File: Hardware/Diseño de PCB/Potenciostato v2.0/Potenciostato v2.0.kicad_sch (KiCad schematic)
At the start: 31 parts, among them J1 Conn_Coaxial, J2 Conn_02x15_Odd_Even, J3 Conn_Coaxial, J5 Conn_Coaxial, J7 USB_B_Micro, U6 AMS1117-3.3, U7 AMS1117-5.0

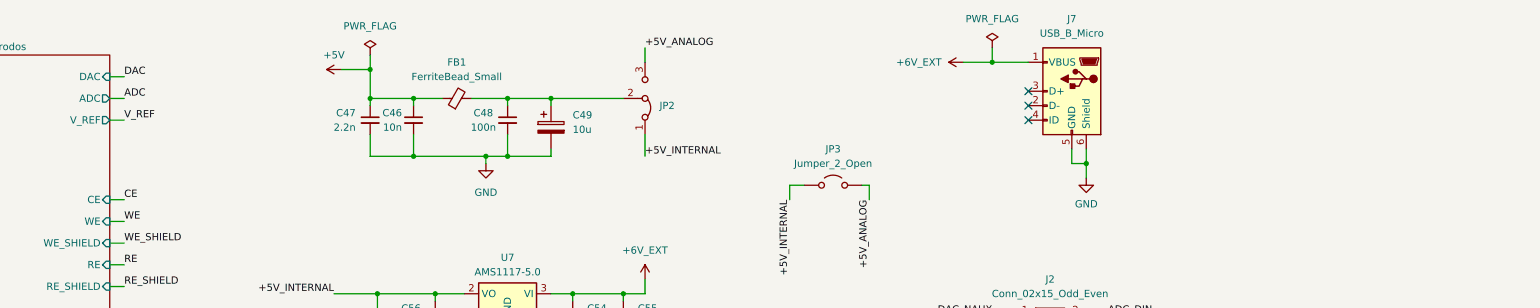
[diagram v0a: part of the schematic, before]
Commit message: Big commit. Hardware was already ready. Board arrived. Hardware testing phase and software development is ongoing, some hardware issues were detected and noted down in the KiCad project for future versions and design corrections. First software libraries under development for ADC, GPIO, Muxes and DAC managment (ADS1255, MAX5217, MAX4737, MAX4617 and GPIO)
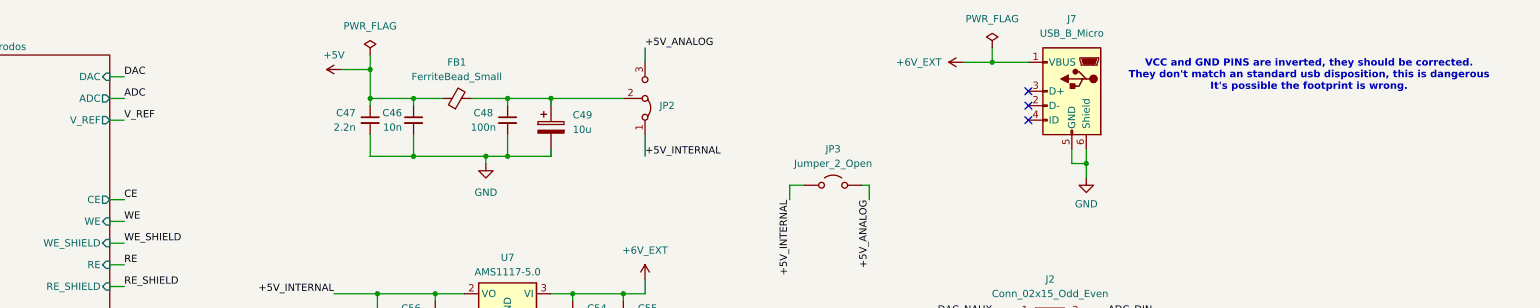
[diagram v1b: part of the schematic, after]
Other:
- note added: "VCC and GND PINS are inverted, they should be corrected. They don't match an standard usb disposition, this is dangerous It's possible the footprint is wrong."
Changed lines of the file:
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@@
 		)
 	)
+	(text "VCC and GND PINS are inverted, they should be corrected.\nThey don't match an standard usb disposition, this is dangerous\nIt's possible the footprint is wrong.\n"
+		(exclude_from_sim no)
+		(at 294.386 28.956 0)
+		(effects
+			(font
+				(size 1.27 1.27)
+				(thickness 0.254)
+				(bold yes)
+				(color 255 0 4 1)
+			)
+		)
+	)
 	(label "DAC_SCL"
 		(at 238.76 73.66 180)
@@
 			)
 		)
-		(pin "CE" input
+		(pin "CE" output
 			(at 83.82 50.8 0)
 			(effects

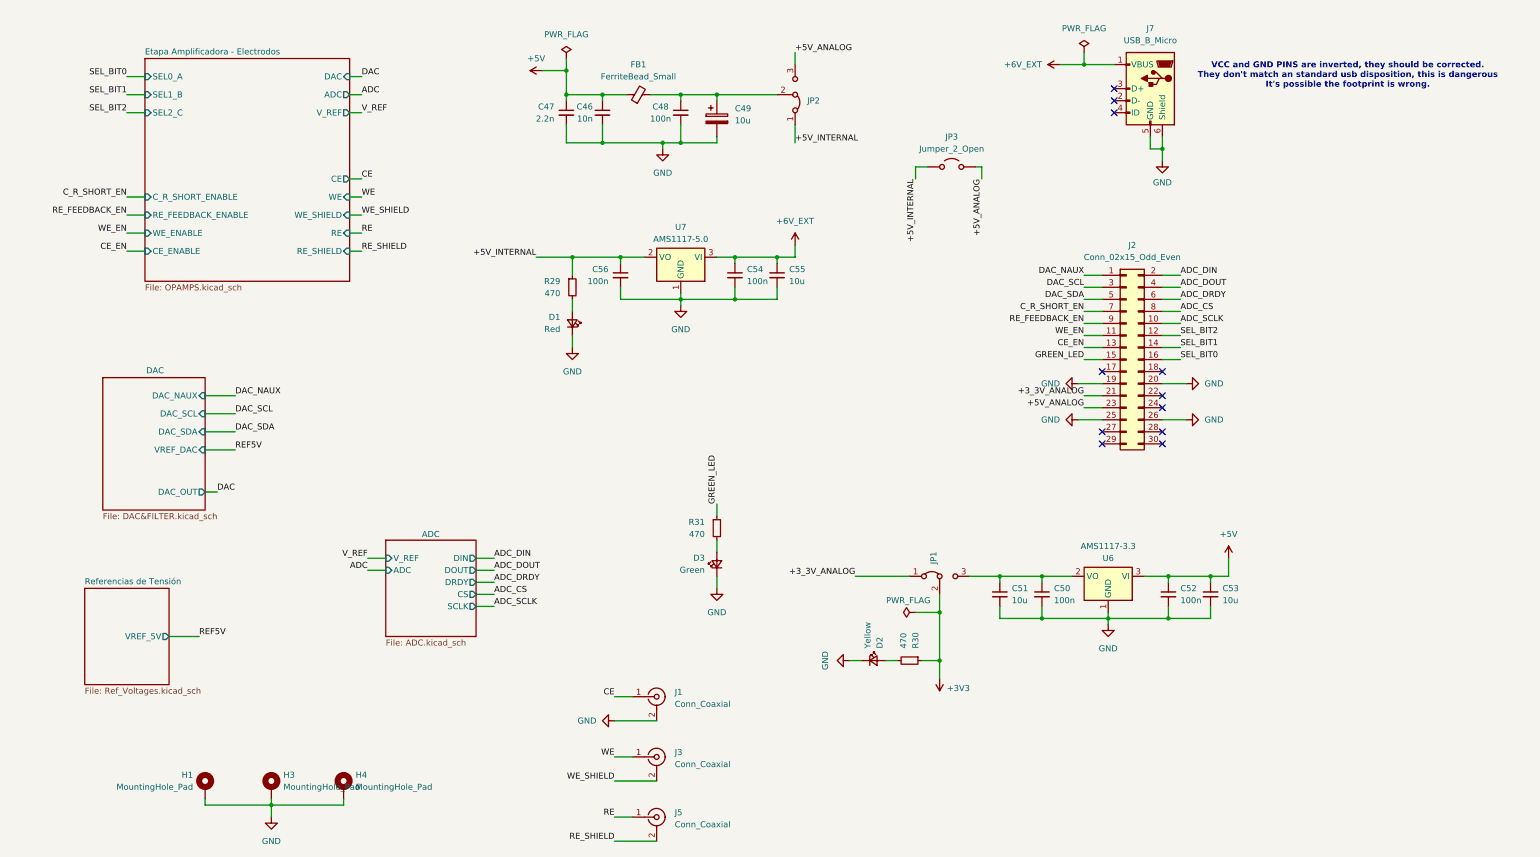
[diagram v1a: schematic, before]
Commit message: Hardware modifications. More notes added to the KiCad project related to hardware issues found during testing. USB Power and ground inverted corrected in design and PCB. MAX4477 replaced by OPA2320 in design and PCB. More notes with recommendations and advised can now be found in the schematics.
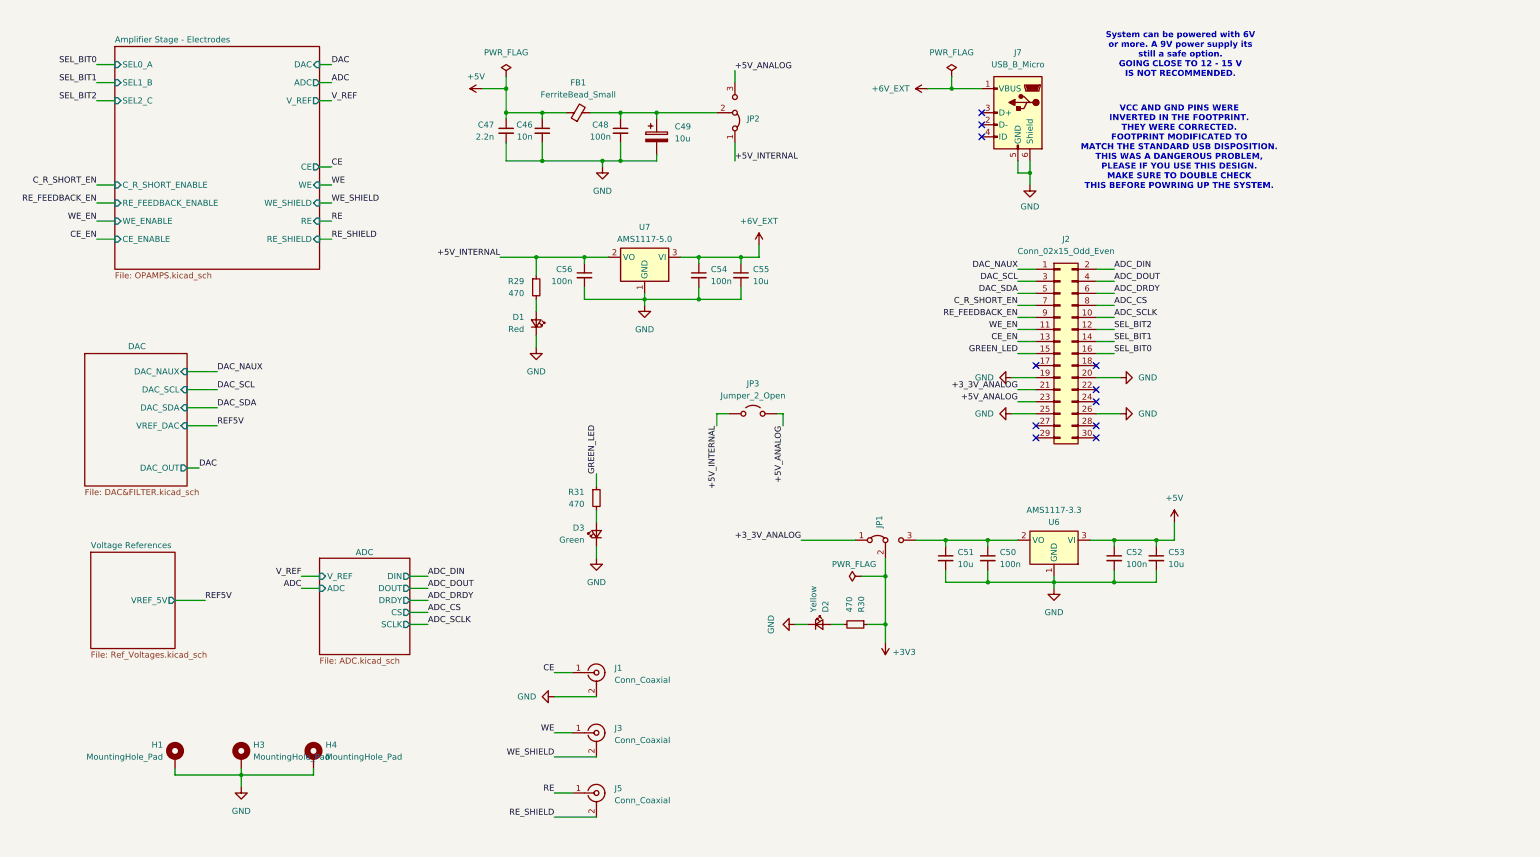
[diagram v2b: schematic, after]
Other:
- sheet Etapa Amplificadora - Electrodos renamed Amplifier Stage - Electrodes
- sheet Referencias de Tensión renamed Voltage References
- note added: "System can be powered with 6V or more. A 9V power supply its still a safe option. GOING CLOSE TO 12 - 15 V IS NOT RECOMMENDED."
- note added: "VCC AND GND PINS WERE INVERTED IN THE FOOTPRINT. THEY WERE CORRECTED. FOOTPRINT MODIFICATED TO MATCH THE STANDARD USB DISPOSITION. THIS WAS A DANGEROUS PROBLEM, PLEASE IF YOU USE THIS DESIGN. MAKE SURE TO DOUBLE CHECK THIS BEFORE POWRING UP THE SYSTEM."
- note removed: "VCC and GND PINS are inverted, they should be corrected. They don't match an standard usb disposition, this is dangerous It's possible the footprint is wrong."
- moved on the sheet: C46, C47, C48, C49, C50, C51, C52, C53, C54, C55, C56, D1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

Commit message: New README update
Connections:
- net SEL_BIT0 renamed SEL_BIT0_A
- net SEL_BIT1 renamed SEL_BIT1_B
- net SEL_BIT2 renamed SEL_BIT2_C
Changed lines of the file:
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@@
 		)
 	)
-	(label "SEL_BIT0"
+	(label "SEL_BIT0_A"
 		(at 245.11 87.63 0)
 		(fields_autoplaced yes)
@@
 		)
 	)
-	(label "SEL_BIT1"
+	(label "SEL_BIT1_B"
 		(at 30.48 30.48 180)
 		(fields_autoplaced yes)
@@
 		)
 	)
-	(label "SEL_BIT1"
+	(label "SEL_BIT1_B"
 		(at 245.11 85.09 0)
 		(fields_autoplaced yes)
@@
 		)
 	)
-	(label "SEL_BIT2"
+	(label "SEL_BIT2_C"
 		(at 30.48 34.29 180)
 		(fields_autoplaced yes)
@@
 		)
 	)
-	(label "SEL_BIT0"
+	(label "SEL_BIT0_A"
 		(at 30.48 26.67 180)
 		(fields_autoplaced yes)
@@
 		)
 	)
-	(label "SEL_BIT2"
+	(label "SEL_BIT2_C"
 		(at 245.11 82.55 0)
 		(fields_autoplaced yes)

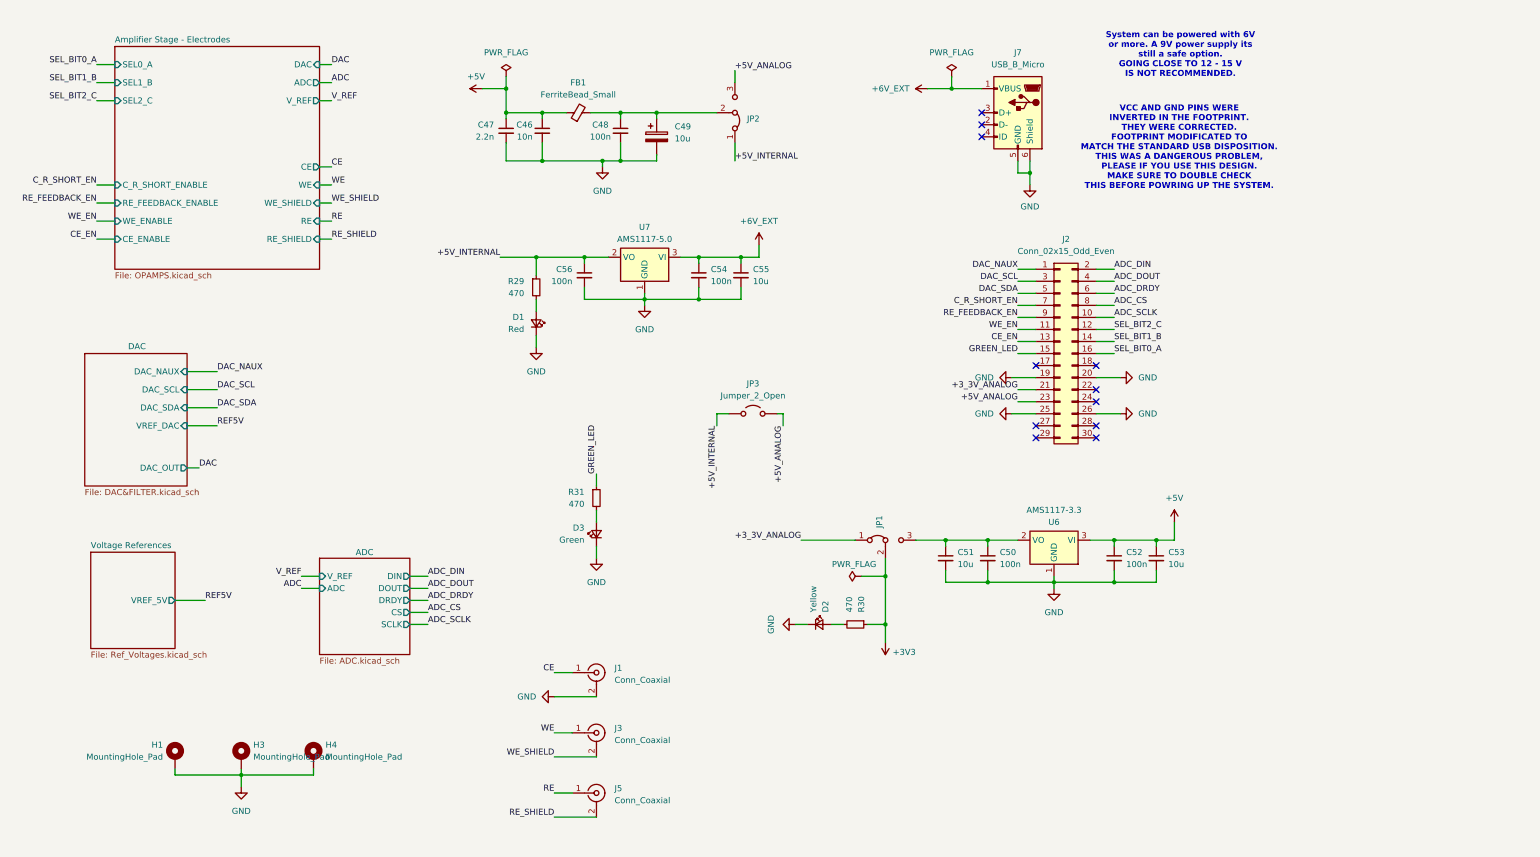
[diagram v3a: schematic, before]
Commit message: Further documentation and notes on the schematic. Software updates: In MAX4617, corrections in write function, more robust code verification to prevent overflows. In MUX, correction to MAX4617 gain codification and pinout updgraded for MAX4737. ADS1255, mux configured to AIN0-AINCOM in ADS_Initialized.
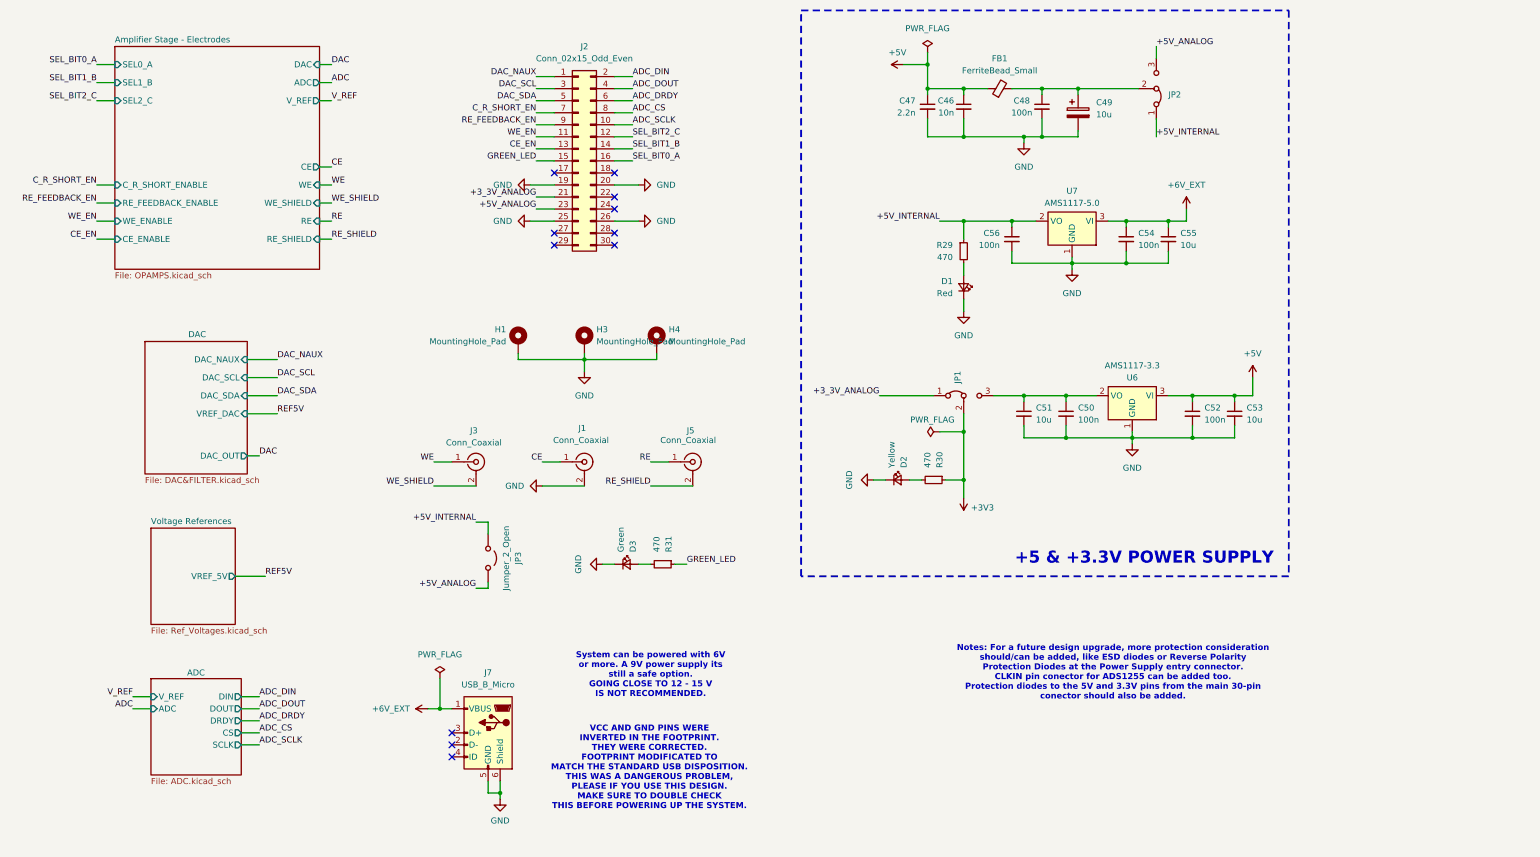
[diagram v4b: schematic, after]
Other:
- note added: "+5 & +3.3V POWER SUPPLY"
- note added: "Notes: For a future design upgrade, more protection consideration should/can be added, like ESD diodes or Reverse Polarity Protection Diodes at the Power Supply entry connector. CLKIN pin conector for ADS1255 can be added too. Protection diodes to the 5V and 3.3V pins from the main 30-pin conector should also be added."
- note added: "VCC AND GND PINS WERE INVERTED IN THE FOOTPRINT. THEY WERE CORRECTED. FOOTPRINT MODIFICATED TO MATCH THE STANDARD USB DISPOSITION. THIS WAS A DANGEROUS PROBLEM, PLEASE IF YOU USE THIS DESIGN. MAKE SURE TO DOUBLE CHECK THIS BEFORE POWERING UP THE SYSTEM."
- note removed: "VCC AND GND PINS WERE INVERTED IN THE FOOTPRINT. THEY WERE CORRECTED. FOOTPRINT MODIFICATED TO MATCH THE STANDARD USB DISPOSITION. THIS WAS A DANGEROUS PROBLEM, PLEASE IF YOU USE THIS DESIGN. MAKE SURE TO DOUBLE CHECK THIS BEFORE POWRING UP THE SYSTEM."
- moved on the sheet: C46, C47, C48, C49, C50, C51, C52, C53, C54, C55, C56, D1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
